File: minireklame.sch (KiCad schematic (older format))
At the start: 54 parts, among them IC1 ATXMEGA64A4U-A, P1 CONN_01X04, P10 CONN_01X04, P11 CONN_01X04, P12 CONN_01X04, P13 CONN_01X04, P14 CONN_01X04, P15 CONN_01X04, P16 CONN_01X04, P17 Screw_Terminal_1x02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

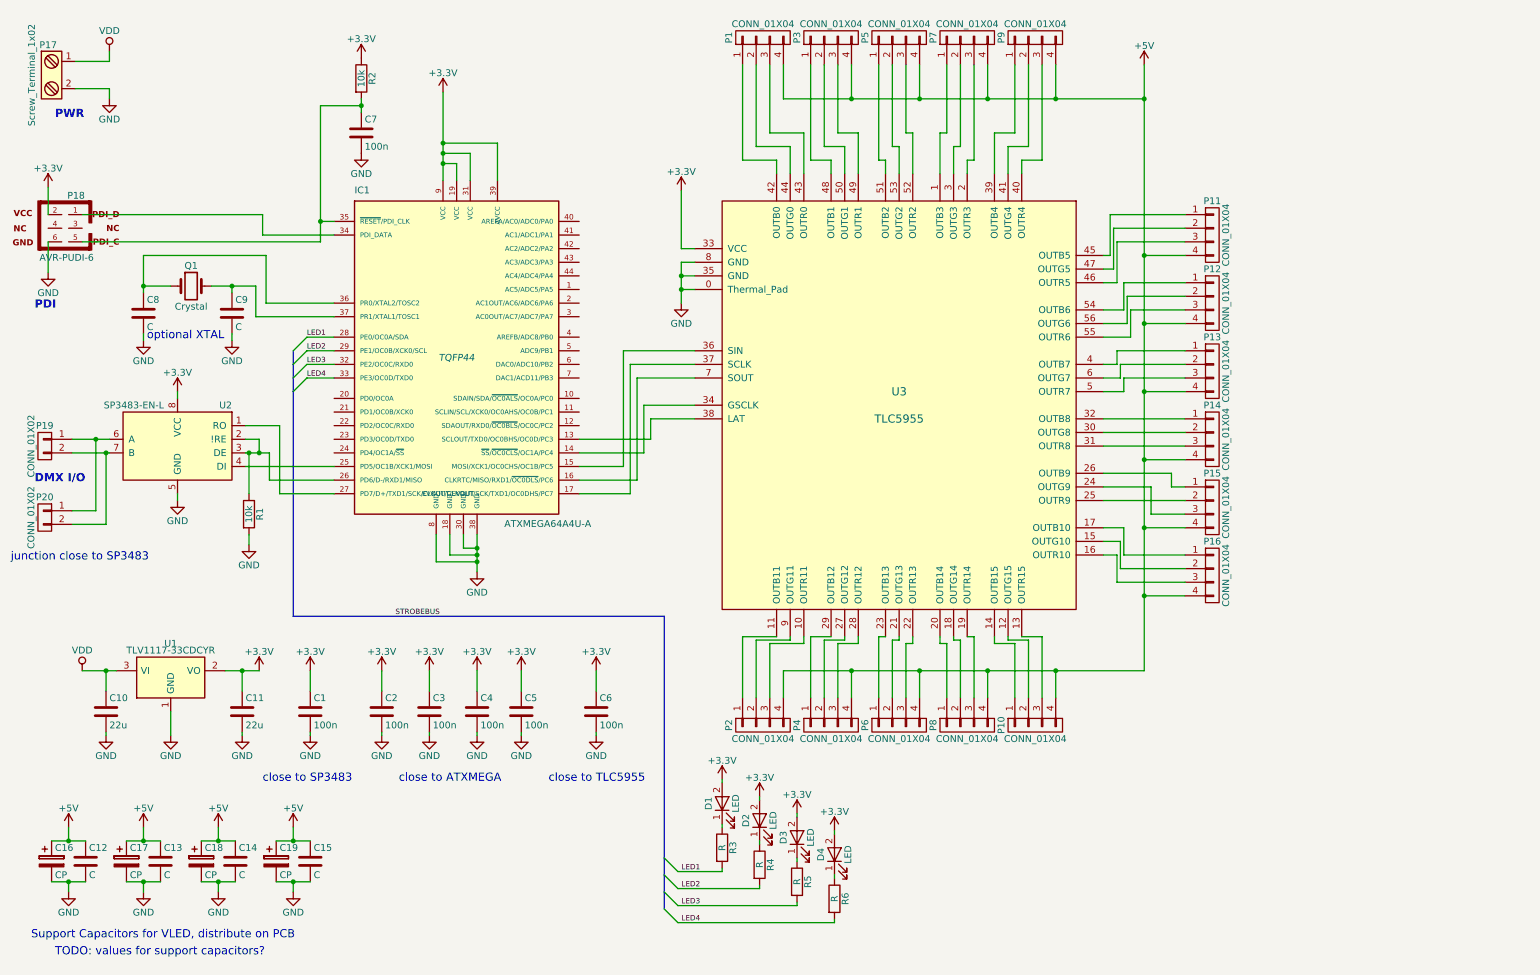
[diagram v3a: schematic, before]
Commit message: Annotating footprints for C, R and ATXMEGA, QFN for TLC5955 needs different pitch
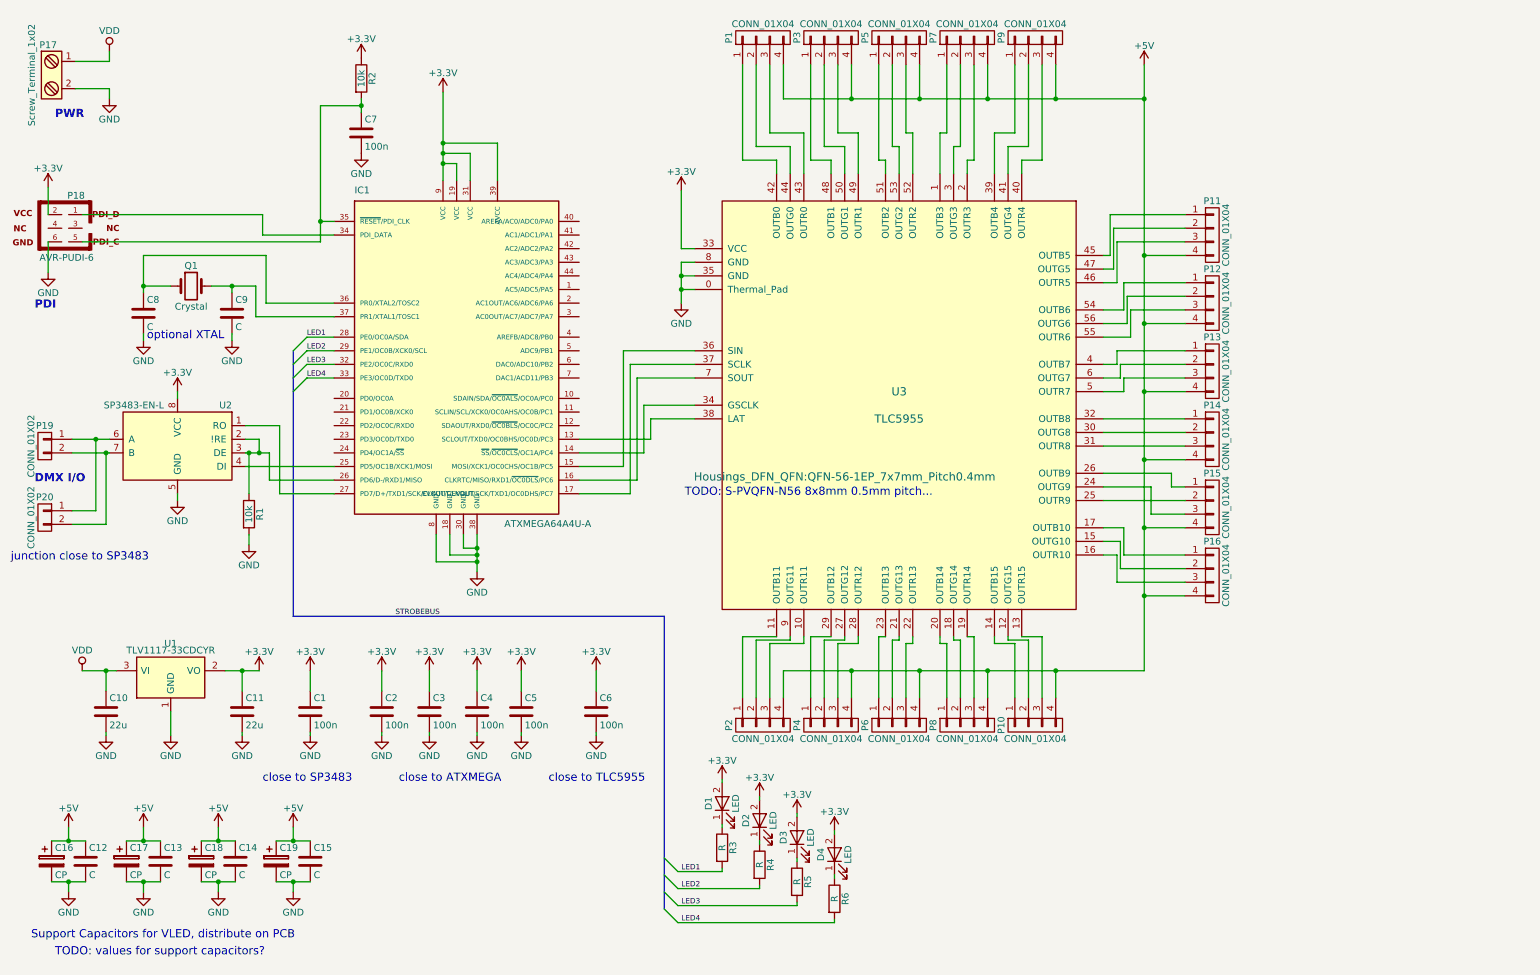
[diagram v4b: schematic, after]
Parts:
- C1, C10, C11, C12, C13, C14, C15, C2, C3, C4, C5, C6, C7, C8, C9: footprint (none) -> Capacitors_SMD:C_0805_HandSoldering
- IC1: footprint TQFP44 -> Housings_QFP:TQFP-44_10x10mm_Pitch0.8mm
- R1, R2, R3, R4, R5, R6: footprint (none) -> Resistors_SMD:R_0805_HandSoldering
- U3: footprint (none) -> Housings_DFN_QFN:QFN-56-1EP_7x7mm_Pitch0.4mm
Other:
- note added: "TODO: S-PVQFN-N56 8x8mm 0.5mm pitch..."

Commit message: adding JST GH BM series connector to all normal pin connectors
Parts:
- P1, P10, P11, P12, P13, P14, P15, P16, P2, P3, P4, P5, P6, P7, P8, P9: footprint (none) -> Connectors_JST:JST_GH_BM04B-GHS-TBT_04x1.25mm_Straight
- P19, P20: footprint (none) -> Connectors_JST:JST_GH_BM02B-GHS-TBT_02x1.25mm_Straight
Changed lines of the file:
@@
 F 0 "P1" H 6100 1200 50  0000 C CNN
 F 1 "CONN_01X04" V 6200 950 50  0000 C CNN
-F 2 "" H 6100 950 50  0000 C CNN
+F 2 "Connectors_JST:JST_GH_BM04B-GHS-TBT_04x1.25mm_Straight" H 6100 950 50  0001 C CNN
 F 3 "" H 6100 950 50  0000 C CNN
 F 4 "B4B-PH-K-S(LF)(SN)" H 6100 950 60  0001 C CNN "manf#"
@@
 F 0 "P3" H 6600 1200 50  0000 C CNN
 F 1 "CONN_01X04" V 6700 950 50  0000 C CNN
-F 2 "" H 6600 950 50  0000 C CNN
+F 2 "Connectors_JST:JST_GH_BM04B-GHS-TBT_04x1.25mm_Straight" H 6600 950 50  0001 C CNN
 F 3 "" H 6600 950 50  0000 C CNN
 	1    6600 950
@@
 F 0 "P5" H 7100 1200 50  0000 C CNN
 F 1 "CONN_01X04" V 7200 950 50  0000 C CNN
-F 2 "" H 7100 950 50  0000 C CNN
+F 2 "Connectors_JST:JST_GH_BM04B-GHS-TBT_04x1.25mm_Straight" H 7100 950 50  0001 C CNN
 F 3 "" H 7100 950 50  0000 C CNN
 	1    7100 950
@@
 F 0 "P9" H 8100 1200 50  0000 C CNN
 F 1 "CONN_01X04" V 8200 950 50  0000 C CNN
-F 2 "" H 8100 950 50  0000 C CNN
+F 2 "Connectors_JST:JST_GH_BM04B-GHS-TBT_04x1.25mm_Straight" H 8100 950 50  0001 C CNN
 F 3 "" H 8100 950 50  0000 C CNN
 	1    8100 950
@@
 F 0 "P7" H 7600 1200 50  0000 C CNN
 F 1 "CONN_01X04" V 7700 950 50  0000 C CNN
-F 2 "" H 7600 950 50  0000 C CNN
+F 2 "Connectors_JST:JST_GH_BM04B-GHS-TBT_04x1.25mm_Straight" H 7600 950 50  0001 C CNN
 F 3 "" H 7600 950 50  0000 C CNN
 	1    7600 950
@@
 F 0 "P11" H 9400 2650 50  0000 C CNN
 F 1 "CONN_01X04" V 9500 2400 50  0000 C CNN
-F 2 "" H 9400 2400 50  0000 C CNN
+F 2 "Connectors_JST:JST_GH_BM04B-GHS-TBT_04x1.25mm_Straight" H 9400 2400 50  0001 C CNN
 F 3 "" H 9400 2400 50  0000 C CNN
 	1    9400 2400
@@
 F 0 "P13" H 9400 3650 50  0000 C CNN
 F 1 "CONN_01X04" V 9500 3400 50  0000 C CNN
-F 2 "" H 9400 3400 50  0000 C CNN
+F 2 "Connectors_JST:JST_GH_BM04B-GHS-TBT_04x1.25mm_Straight" H 9400 3400 50  0001 C CNN
 F 3 "" H 9400 3400 50  0000 C CNN
 	1    9400 3400
@@
 F 0 "P12" H 9400 3150 50  0000 C CNN
 F 1 "CONN_01X04" V 9500 2900 50  0000 C CNN
-F 2 "" H 9400 2900 50  0000 C CNN
+F 2 "Connectors_JST:JST_GH_BM04B-GHS-TBT_04x1.25mm_Straight" H 9400 2900 50  0001 C CNN
 F 3 "" H 9400 2900 50  0000 C CNN
 	1    9400 2900
@@
 F 0 "P16" H 9400 5150 50  0000 C CNN
 F 1 "CONN_01X04" V 9500 4900 50  0000 C CNN
-F 2 "" H 9400 4900 50  0000 C CNN
+F 2 "Connectors_JST:JST_GH_BM04B-GHS-TBT_04x1.25mm_Straight" H 9400 4900 50  0001 C CNN
 F 3 "" H 9400 4900 50  0000 C CNN
 	1    9400 4900
@@
 F 0 "P15" H 9400 4650 50  0000 C CNN
 F 1 "CONN_01X04" V 9500 4400 50  0000 C CNN
-F 2 "" H 9400 4400 50  0000 C CNN
+F 2 "Connectors_JST:JST_GH_BM04B-GHS-TBT_04x1.25mm_Straight" H 9400 4400 50  0001 C CNN
 F 3 "" H 9400 4400 50  0000 C CNN
 	1    9400 4400
@@
 F 0 "P14" H 9400 4150 50  0000 C CNN
 F 1 "CONN_01X04" V 9500 3900 50  0000 C CNN
-F 2 "" H 9400 3900 50  0000 C CNN
+F 2 "Connectors_JST:JST_GH_BM04B-GHS-TBT_04x1.25mm_Straight" H 9400 3900 50  0001 C CNN
 F 3 "" H 9400 3900 50  0000 C CNN
 	1    9400 3900
@@
 F 0 "P10" H 8100 6250 50  0000 C CNN
 F 1 "CONN_01X04" V 8200 6000 50  0000 C CNN
-F 2 "" H 8100 6000 50  0000 C CNN
+F 2 "Connectors_JST:JST_GH_BM04B-GHS-TBT_04x1.25mm_Straight" H 8100 6000 50  0001 C CNN
 F 3 "" H 8100 6000 50  0000 C CNN
 	1    8100 6000
@@
 F 0 "P8" H 7600 6250 50  0000 C CNN
 F 1 "CONN_01X04" V 7700 6000 50  0000 C CNN
-F 2 "" H 7600 6000 50  0000 C CNN
+F 2 "Connectors_JST:JST_GH_BM04B-GHS-TBT_04x1.25mm_Straight" H 7600 6000 50  0001 C CNN
 F 3 "" H 7600 6000 50  0000 C CNN
 	1    7600 6000
@@
 F 0 "P6" H 7100 6250 50  0000 C CNN
 F 1 "CONN_01X04" V 7200 6000 50  0000 C CNN
-F 2 "" H 7100 6000 50  0000 C CNN
+F 2 "Connectors_JST:JST_GH_BM04B-GHS-TBT_04x1.25mm_Straight" H 7100 6000 50  0001 C CNN
 F 3 "" H 7100 6000 50  0000 C CNN
 	1    7100 6000
@@
 F 0 "P4" H 6600 6250 50  0000 C CNN
 F 1 "CONN_01X04" V 6700 6000 50  0000 C CNN
-F 2 "" H 6600 6000 50  0000 C CNN
+F 2 "Connectors_JST:JST_GH_BM04B-GHS-TBT_04x1.25mm_Straight" H 6600 6000 50  0001 C CNN
 F 3 "" H 6600 6000 50  0000 C CNN
 	1    6600 6000
@@
 F 0 "P2" H 6100 6250 50  0000 C CNN
 F 1 "CONN_01X04" V 6200 6000 50  0000 C CNN
-F 2 "" H 6100 6000 50  0000 C CNN
+F 2 "Connectors_JST:JST_GH_BM04B-GHS-TBT_04x1.25mm_Straight" H 6100 6000 50  0001 C CNN
 F 3 "" H 6100 6000 50  0000 C CNN
 	1    6100 6000
@@
 F 0 "P19" H 825 4100 50  0000 C CNN
 F 1 "CONN_01X02" V 925 3950 50  0000 C CNN
-F 2 "" H 825 3950 50  0000 C CNN
+F 2 "Connectors_JST:JST_GH_BM02B-GHS-TBT_02x1.25mm_Straight" H 825 3950 50  0001 C CNN
 F 3 "" H 825 3950 50  0000 C CNN
 	1    825  3950
@@
 F 0 "P20" H 825 4625 50  0000 C CNN
 F 1 "CONN_01X02" V 925 4475 50  0000 C CNN
-F 2 "" H 825 4475 50  0000 C CNN
+F 2 "Connectors_JST:JST_GH_BM02B-GHS-TBT_02x1.25mm_Straight" H 825 4475 50  0001 C CNN
 F 3 "" H 825 4475 50  0000 C CNN
 	1    825  4475

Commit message: Annotating footprints for electrolyte Cs, LEDs and crystal
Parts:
- C16, C17, C18, C19: footprint (none) -> Capacitors_SMD:CP_Elec_6.3x7.7
- D1, D2, D3, D4: footprint (none) -> LEDs:LED_0805
- P17: footprint (none) -> Connectors_Terminal_Blocks:TerminalBlock_Pheonix_PT-3.5mm_2pol
- P18: footprint AVR-PUDI-6 -> Connectors:IDC_Header_Straight_6pins
- Q1: footprint (none) -> Crystals:Crystal_SMD_3225-4pin_3.2x2.5mm_HandSoldering
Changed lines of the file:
@@
 F 0 "P18" H 895 2590 50  0000 C CNN
 F 1 "AVR-PUDI-6" H 765 2105 50  0000 L BNN
-F 2 "AVR-PUDI-6" V 530 2385 50  0001 C CNN
+F 2 "Connectors:IDC_Header_Straight_6pins" V 530 2385 50  0001 C CNN
 F 3 "" H 975 2350 50  0001 C CNN
 	1    975  2350
@@
 F 0 "Q1" H 1900 2925 50  0000 C CNN
 F 1 "Crystal" H 1900 2625 50  0000 C CNN
-F 2 "" H 1900 2775 50  0001 C CNN
+F 2 "Crystals:Crystal_SMD_3225-4pin_3.2x2.5mm_HandSoldering" H 1900 2775 50  0001 C CNN
 F 3 "" H 1900 2775 50  0001 C CNN
 	1    1900 2775
@@
 F 0 "P17" H 850 1475 50  0000 C TNN
 F 1 "Screw_Terminal_1x02" V 700 1225 50  0000 C TNN
-F 2 "" H 850 1000 50  0001 C CNN
+F 2 "Connectors_Terminal_Blocks:TerminalBlock_Pheonix_PT-3.5mm_2pol" H 850 1000 50  0001 C CNN
 F 3 "" H 825 1225 50  0001 C CNN
 	1    850  1225
@@
 F 0 "C17" H 1450 7100 50  0000 L CNN
 F 1 "CP" H 1450 6900 50  0000 L CNN
-F 2 "" H 1463 6850 50  0001 C CNN
+F 2 "Capacitors_SMD:CP_Elec_6.3x7.7" H 1463 6850 50  0001 C CNN
 F 3 "" H 1425 7000 50  0001 C CNN
 	1    1425 7000
@@
 F 0 "C18" H 2000 7100 50  0000 L CNN
 F 1 "CP" H 2000 6900 50  0000 L CNN
-F 2 "" H 2013 6850 50  0001 C CNN
+F 2 "Capacitors_SMD:CP_Elec_6.3x7.7" H 2013 6850 50  0001 C CNN
 F 3 "" H 1975 7000 50  0001 C CNN
 	1    1975 7000
@@
 F 0 "C16" H 900 7100 50  0000 L CNN
 F 1 "CP" H 900 6900 50  0000 L CNN
-F 2 "" H 913 6850 50  0001 C CNN
+F 2 "Capacitors_SMD:CP_Elec_6.3x7.7" H 913 6850 50  0001 C CNN
 F 3 "" H 875 7000 50  0001 C CNN
 	1    875  7000
@@
 F 0 "C19" H 2550 7100 50  0000 L CNN
 F 1 "CP" H 2550 6900 50  0000 L CNN
-F 2 "" H 2563 6850 50  0001 C CNN
+F 2 "Capacitors_SMD:CP_Elec_6.3x7.7" H 2563 6850 50  0001 C CNN
 F 3 "" H 2525 7000 50  0001 C CNN
 	1    2525 7000
@@
 F 0 "D1" H 5800 6675 50  0000 C CNN
 F 1 "LED" H 5800 6475 50  0000 C CNN
-F 2 "" H 5800 6575 50  0001 C CNN
+F 2 "LEDs:LED_0805" H 5800 6575 50  0001 C CNN
 F 3 "" H 5800 6575 50  0001 C CNN
 	1    5800 6575
@@
 F 0 "D2" H 6075 6800 50  0000 C CNN
 F 1 "LED" H 6075 6600 50  0000 C CNN
-F 2 "" H 6075 6700 50  0001 C CNN
+F 2 "LEDs:LED_0805" H 6075 6700 50  0001 C CNN
 F 3 "" H 6075 6700 50  0001 C CNN
 	1    6075 6700
@@
 F 0 "D3" H 6350 6925 50  0000 C CNN
 F 1 "LED" H 6350 6725 50  0000 C CNN
-F 2 "" H 6350 6825 50  0001 C CNN
+F 2 "LEDs:LED_0805" H 6350 6825 50  0001 C CNN
 F 3 "" H 6350 6825 50  0001 C CNN
 	1    6350 6825
@@
 F 0 "D4" H 6625 7050 50  0000 C CNN
 F 1 "LED" H 6625 6850 50  0000 C CNN
-F 2 "" H 6625 6950 50  0001 C CNN
+F 2 "LEDs:LED_0805" H 6625 6950 50  0001 C CNN
 F 3 "" H 6625 6950 50  0001 C CNN
 	1    6625 6950

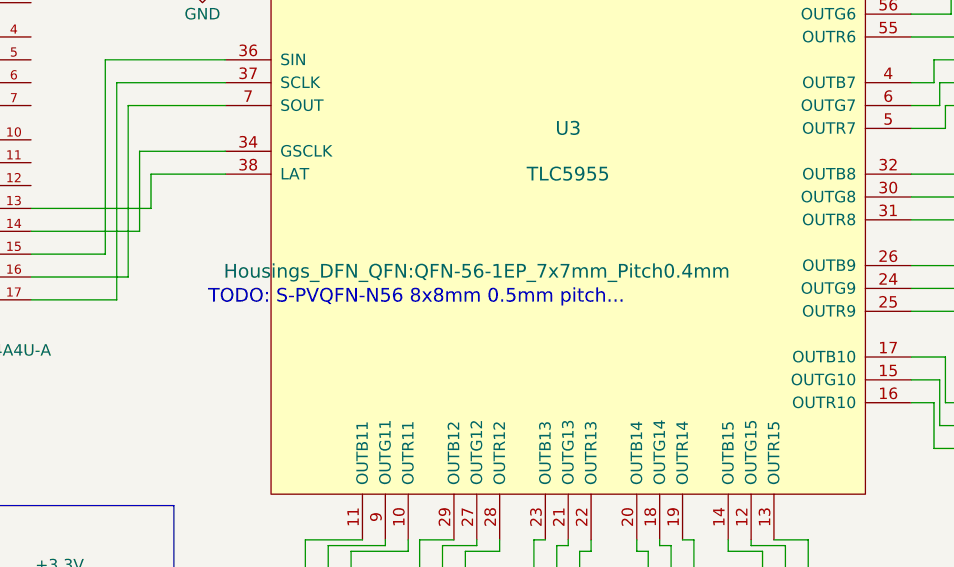
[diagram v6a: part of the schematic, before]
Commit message: Assigning QFP_56_8x8mm_0.5mm_pitch footprint to TLC5955
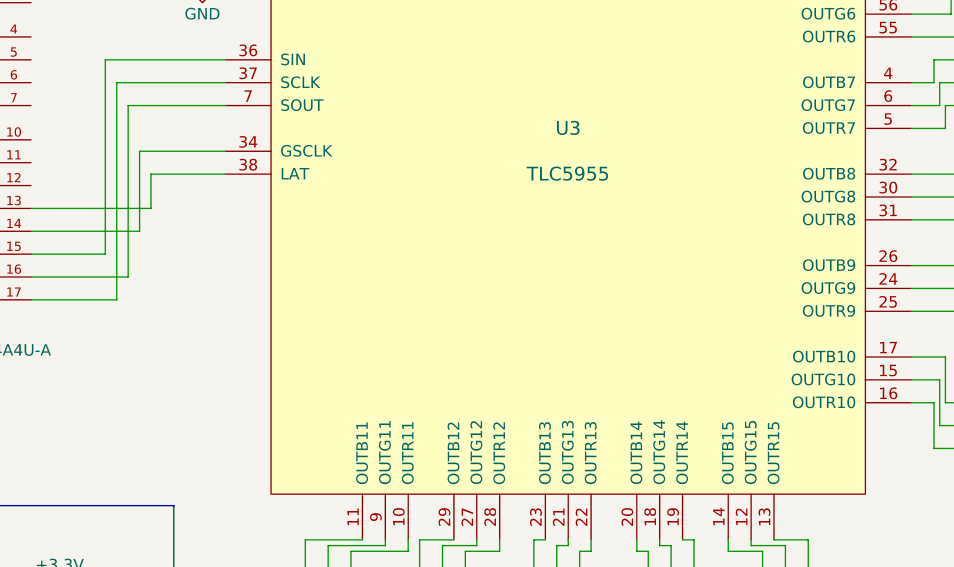
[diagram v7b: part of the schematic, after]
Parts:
- U3: footprint Housings_DFN_QFN:QFN-56-1EP_7x7mm_Pitch0.4mm -> tlc5955:QFP_56_8x8mm_0.5mm_pitch
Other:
- note removed: "TODO: S-PVQFN-N56 8x8mm 0.5mm pitch..."
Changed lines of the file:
@@
 F 0 "U3" H 7100 3750 60  0000 C CNN
 F 1 "TLC5955" H 7100 3550 60  0000 C CNN
-F 2 "Housings_DFN_QFN:QFN-56-1EP_7x7mm_Pitch0.4mm" H 6700 3125 60  0000 C CNN
+F 2 "tlc5955:QFP_56_8x8mm_0.5mm_pitch" H 6700 3125 60  0001 C CNN
 F 3 "" H 7100 3650 60  0000 C CNN
 F 4 "TLC5955DCA" H 7100 3650 60  0001 C CNN "manf#"
@@
 Wire Wire Line
 	5225 4000 4750 4000
-Text Notes 5525 4325 0    60   ~ 0
-TODO: S-PVQFN-N56 8x8mm 0.5mm pitch...
 $EndSCHEMATC
